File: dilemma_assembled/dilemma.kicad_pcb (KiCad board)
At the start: 2 copper layers, 134.1 x 110.3 mm, 124 parts, among them J1 USB_C_Receptacle_USB2.0, J102 Serial, J103 Serial, J105 Conn_01x04_Female, J107 Conn_01x08_Female, J108 Conn_01x01_Female, J109 Conn_01x01_Female, J113 Cirque, J5 Conn_01x02, SW1 SW_Push, SW101 SW_Push, SW102 SW_Push, SW103 SW_Push, SW104 SW_Push, SW105 SW_Push, SW106 SW_Push, SW107 SW_Push, SW108 SW_Push, SW109 SW_Push, SW110 SW_SPST, SW111 SW_SPST, SW112 SW_Push, SW113 SW_Push, SW114 SW_Push, SW115 SW_Push, SW116 SW_Push, SW117 SW_Push, SW118 SW_Push, SW119 locked, SW2 SW_Push, U1 RP2040, U2 GD25Q80CEIGR, U3 XC6210B332MR-G, Y1 Crystal_GND24

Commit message: silkscreen
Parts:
- G*** (x2): moved to B.Cu
- kibuzzard-61F01A92: moved to F.Cu
- moved G*** 74.7 mm to (69.6, 51.3), turned to 180 degrees
- moved G*** 66.3 mm to (78.3, 51.4), turned to 180 degrees
- moved kibuzzard-61F01A92 4.99 mm to (143.5, 56.7), turned to 90 degrees
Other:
- board text added: "a1.1b"
- board text removed: "a1.1a"

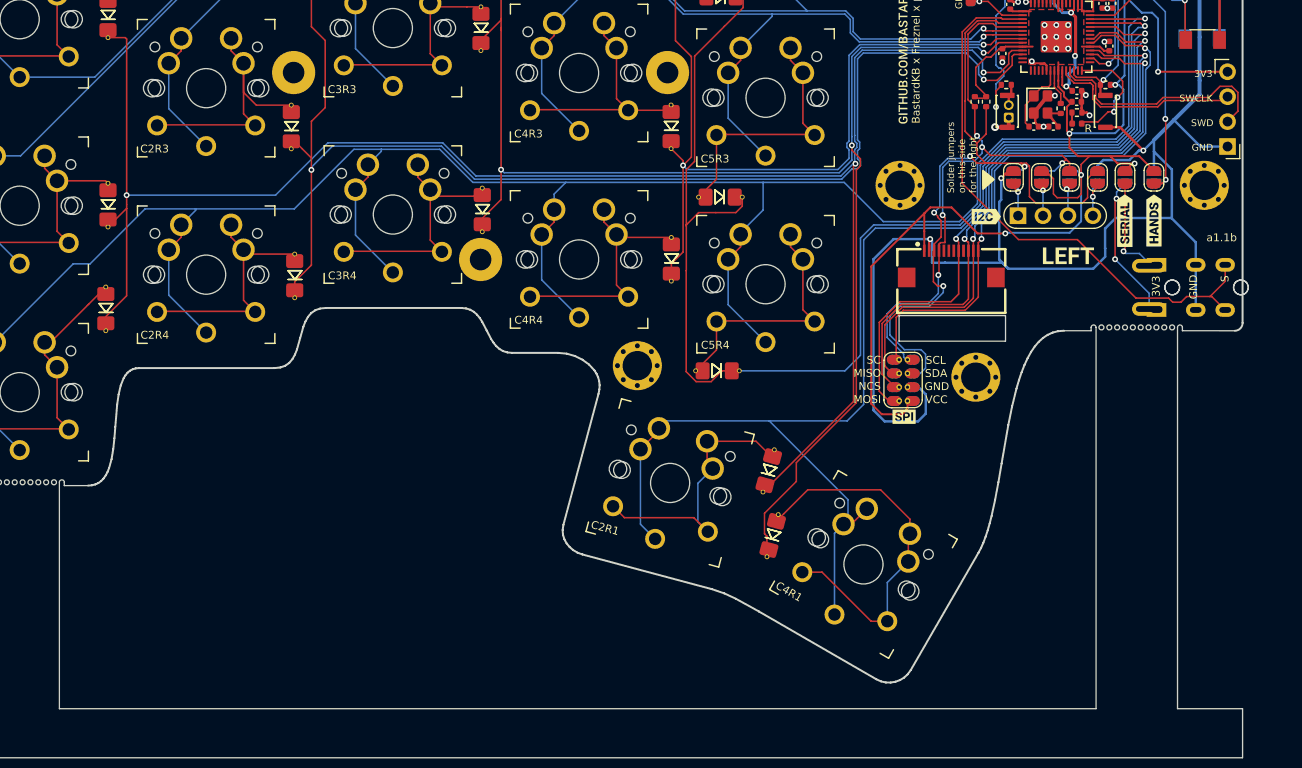
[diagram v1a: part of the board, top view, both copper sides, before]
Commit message: change position of mouse bites
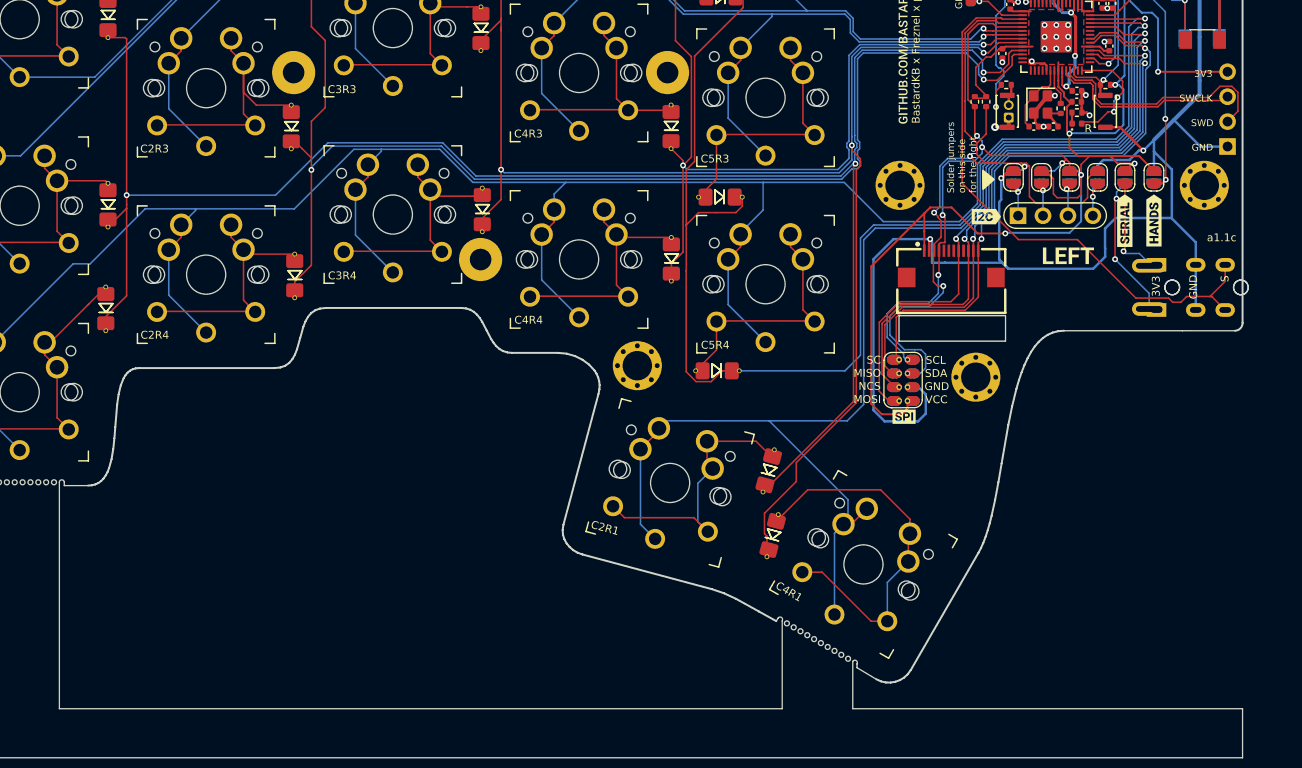
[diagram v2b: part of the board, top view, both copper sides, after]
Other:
- outline, holes or cut-outs redrawn
- board text added: "a1.1c"
- board text removed: "a1.1b"

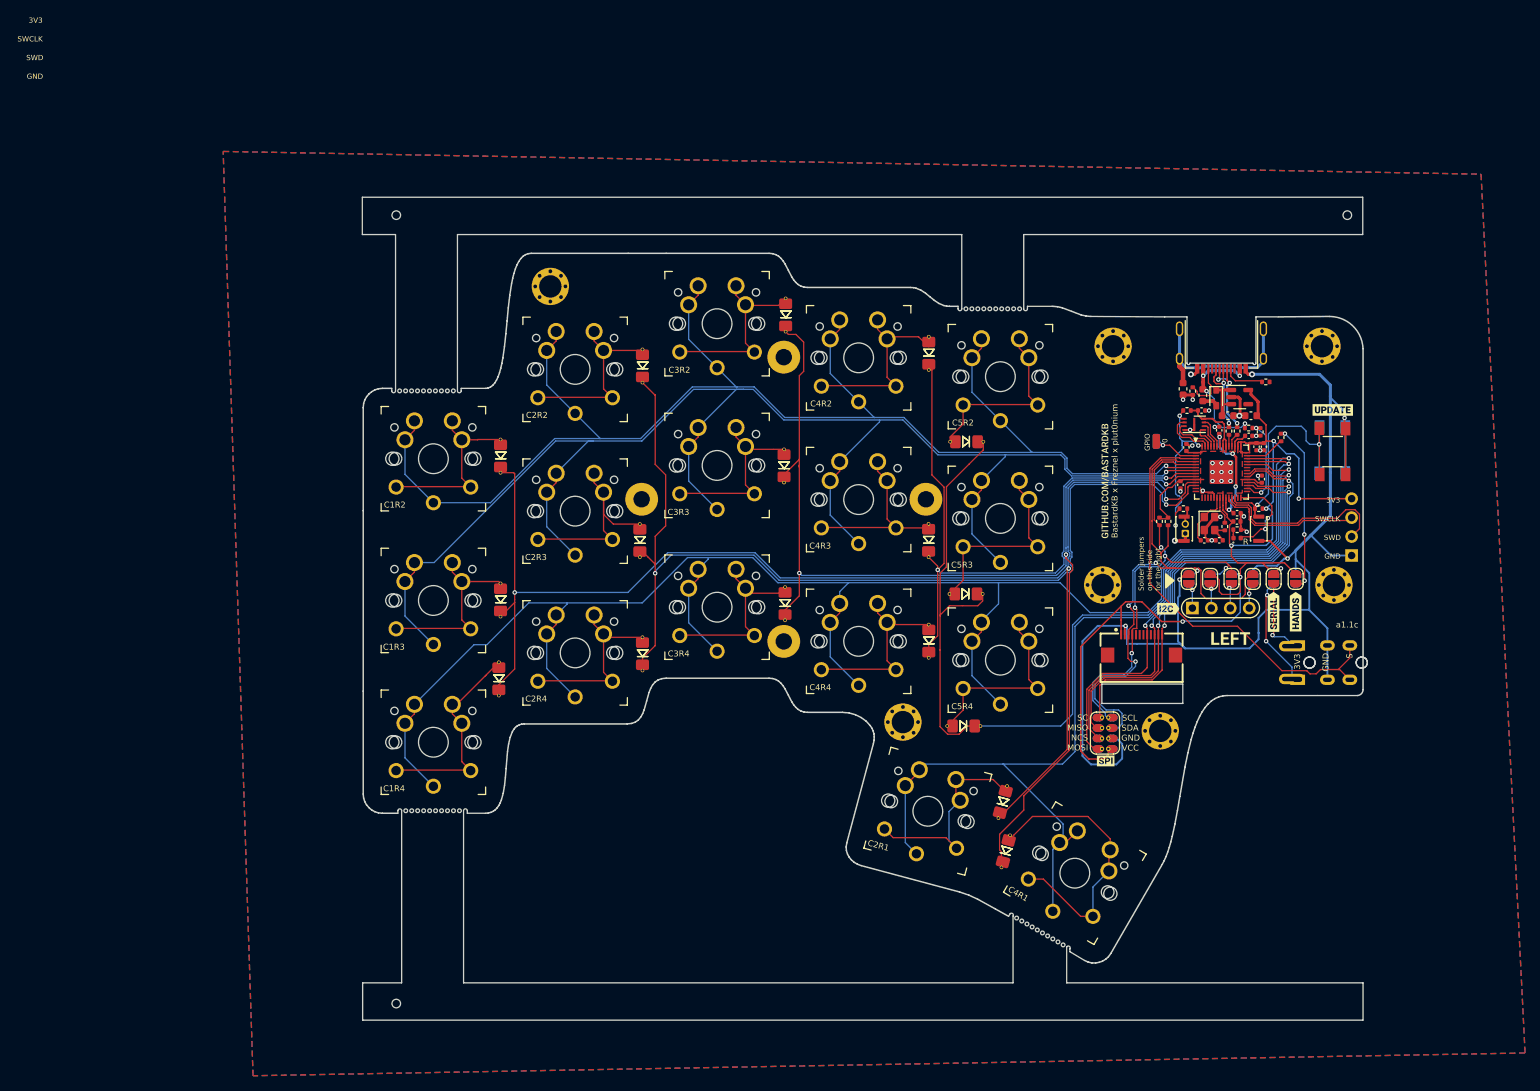
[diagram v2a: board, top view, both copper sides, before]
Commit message: switch up fpc connections
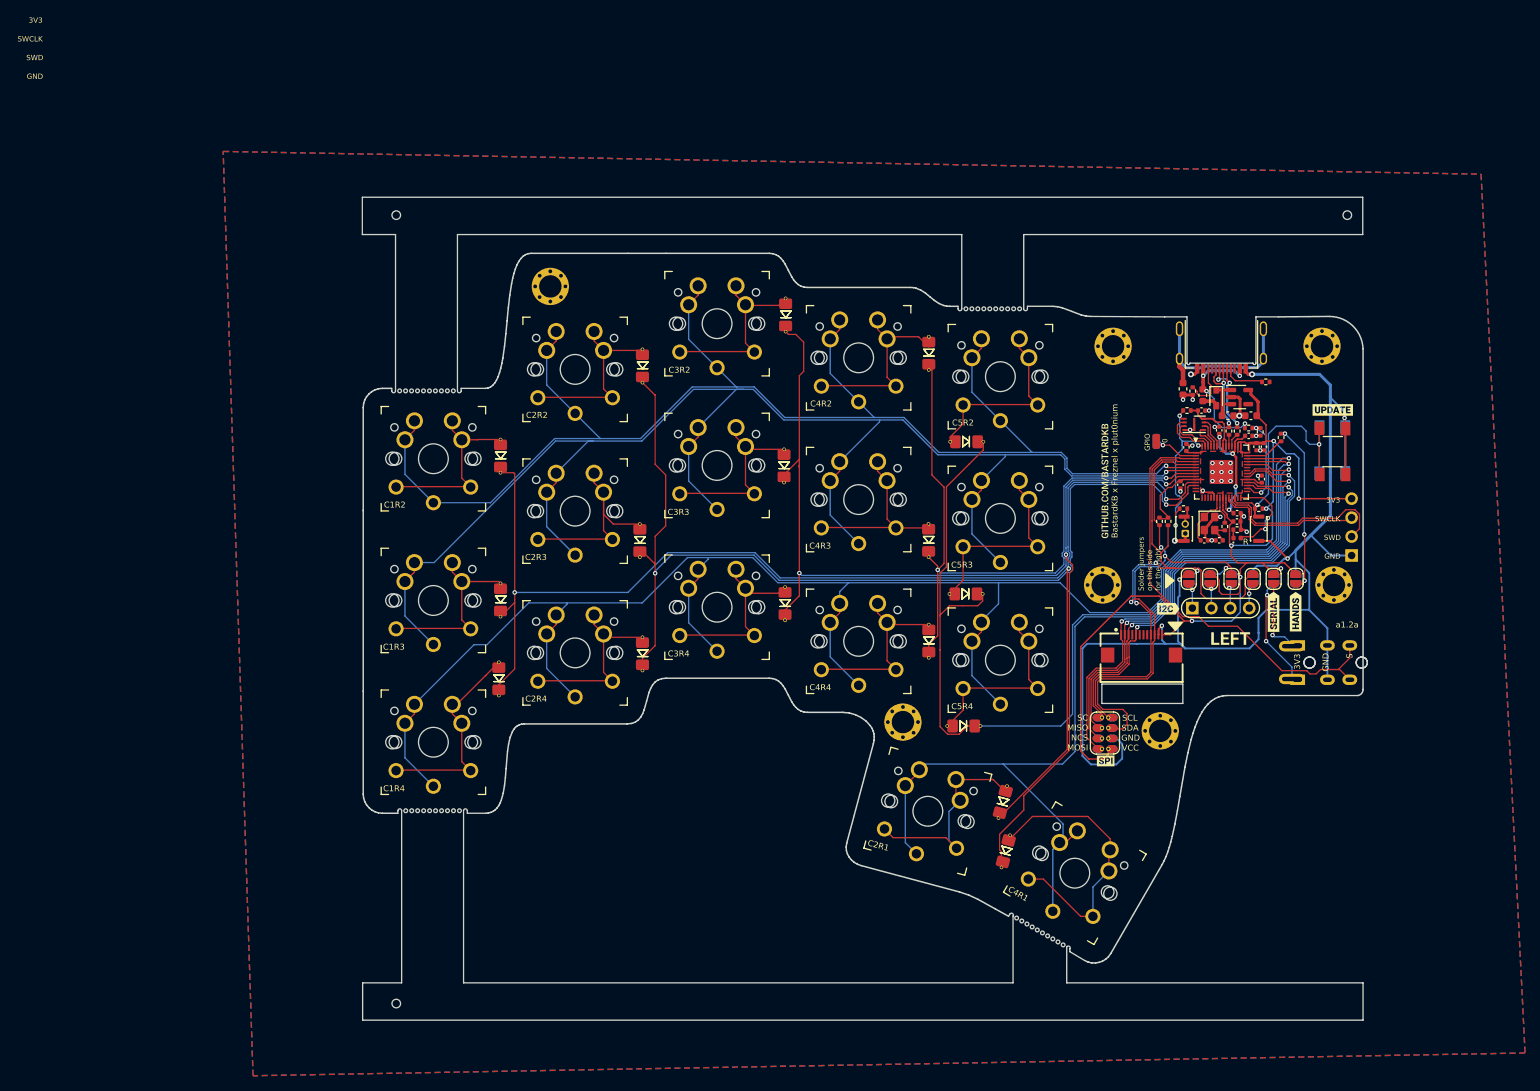
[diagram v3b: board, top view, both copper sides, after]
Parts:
- removed the REF** at (100.4, 59.2)
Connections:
- J107 pad 5: mosi_l -> sc_l
- J107 pad 6: NCS -> miso_l
- J107 pad 7: miso_l -> NCS
- J107 pad 8: sc_l -> mosi_l
- J113 pad 1: +3V3 -> sc_l
- J113 pad 10: NCS -> sda_l
- J113 pad 11: miso_l -> Gnd_l
- J113 pad 12: sc_l -> +3V3
- J113 pad 2: Gnd_l -> miso_l
- J113 pad 3: sda_l -> NCS
- J113 pad 4: scl_l -> unconnected-(J113-Pad4)
- J113 pad 5: unconnected-(J113-Pad5) -> mosi_l
- J113 pad 8: mosi_l -> unconnected-(J113-Pad8)
- J113 pad 9: unconnected-(J113-Pad9) -> scl_l
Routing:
- net sda_l: track 80.7 -> 86.0 mm, vias 4 -> 3
- net mosi_l: track 65.7 -> 60.5 mm
- net sc_l: track 59.8 -> 64.8 mm
- net scl_l: track 62.2 -> 65.2 mm, vias 5 -> 4
- net NCS: track 62.5 -> 60.1 mm
- net Gnd_l: track 202.0 -> 201.0 mm
- net miso_l: track 60.1 -> 61.0 mm
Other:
- board text added: "a1.2a"
- board text removed: "a1.1c"
